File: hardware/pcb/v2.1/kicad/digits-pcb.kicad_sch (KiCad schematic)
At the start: 49 parts, among them J1 Conn_02x20_Odd_Even, J3 VIN_BARREL_PIGTAIL, J4 Conn_01x07, J6 Conn_01x02, J7 Screw_Terminal_01x02, J8 Conn_01x04, SW1 Hook_DPDT, SW2 SW_Push, U1 LM2596S-5, U3 RP2040, U4 W25Q16JVSSIQ, U5 AMS1117-3.3, Y1 ABM8-272-T3

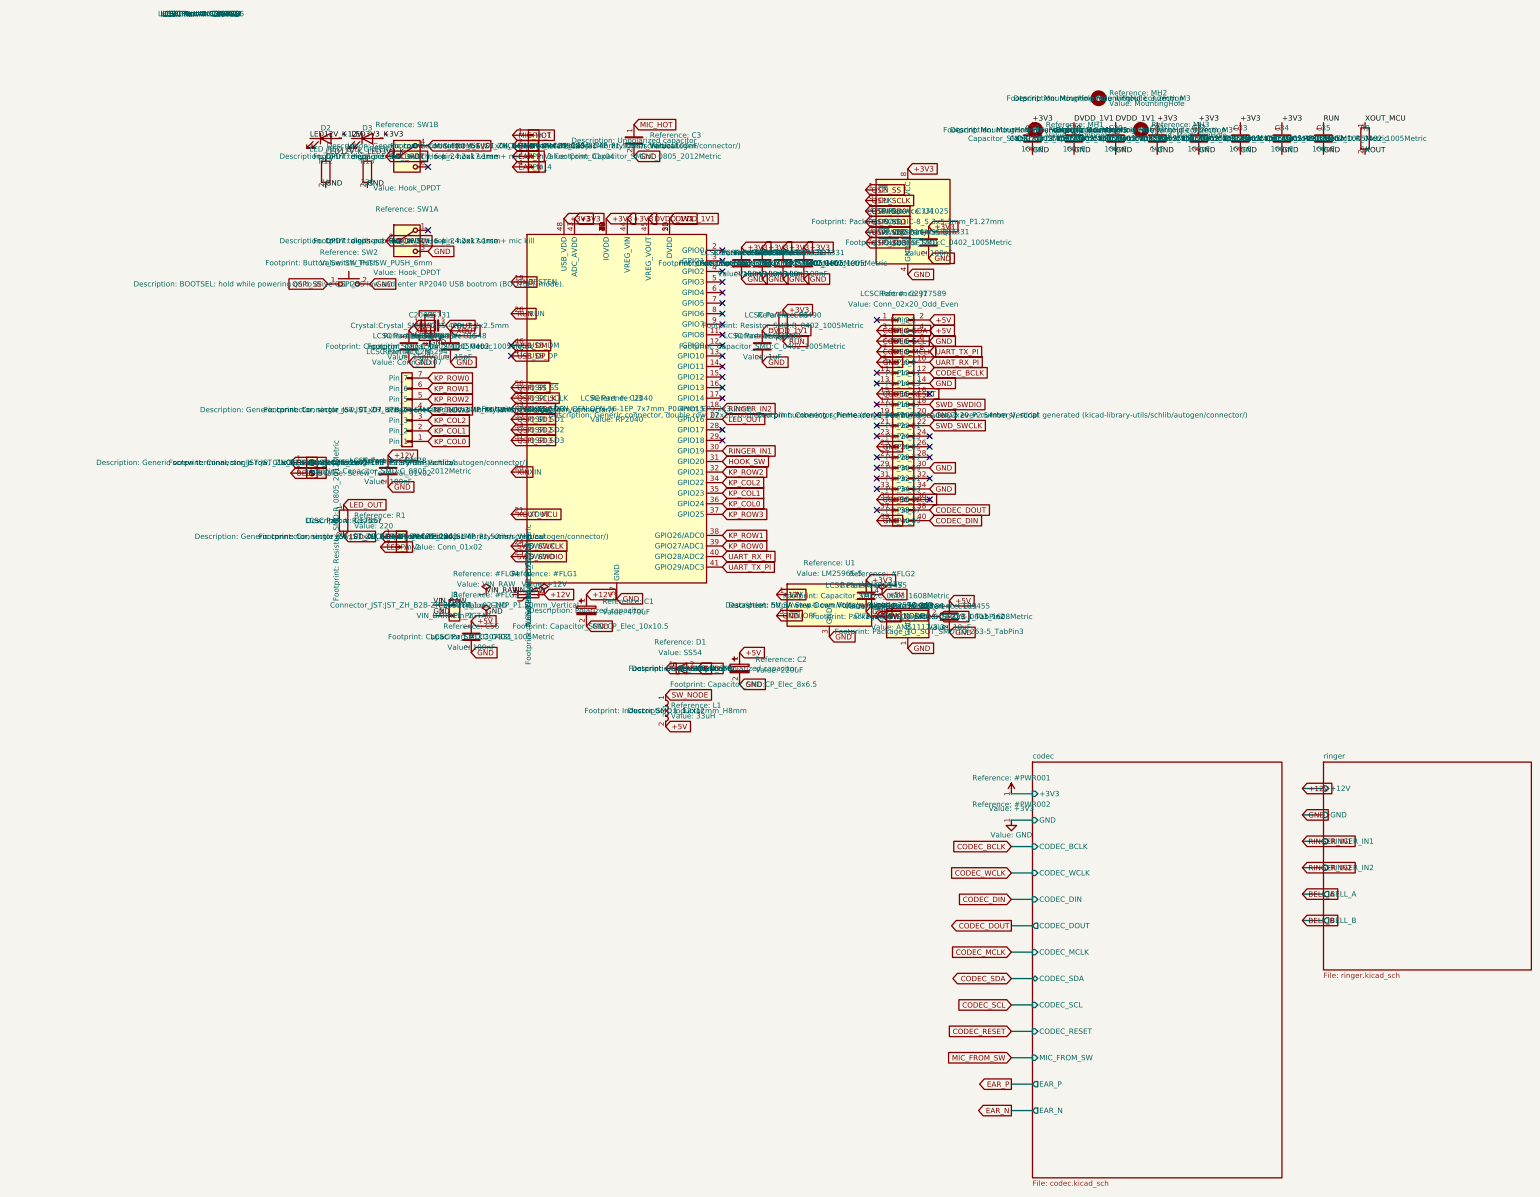
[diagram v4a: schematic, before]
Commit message: feat(hardware): switch to 5V input, drop buck stage, retarget boost to 37V
Bench testing confirmed the on-board boost approach matches the external
transformer for bell loudness: 79 dBA (transformer) vs 78 dBA (boost at 33V),
measured same distance/room/meter. The transformer is no longer justified.

Power input changed from 12V to 5V:
- Removed the entire LM2596 buck stage (U1, L1, D1, C2, C56). With 5V input
  there is nothing to buck down for the Pi; 5V feeds the Pi, the AMS1117 LDO,
  and the XL6019 boost directly.
- Merged the old +12V rail into +5V throughout both sheets.
- J3 connector kept as-is for now (barrel-jack pigtail); it will need a
  higher-current part since 5V at the same power draws ~2x the current.
- R12 (12V power LED resistor) changed 1k -> 300R to rebias for the 5V rail.

Boost output retargeted 42V -> 37V (R20 64.9k -> 57.6k, R21 unchanged at 2k):
- 37V gives 8V margin below the DRV8871's 45V VM limit (was only 3V at 42V).
- Bell already measured 78 dBA at 33V; 37V is marginally louder with far
  better headroom against inductive-kickback spikes.
- Lower boost ratio is also easier on the XL6019 from a 5V input.

PCB: boost cluster (U10/L10/D10/C100/C101/R20/R21) repositioned from the
off-board scratch area into the region between U2 and the codec. All
footprints on F.Cu. Layout and routing still in progress.

ERC clean (0 errors). Netlist: 77 components, +12V net fully eliminated,
codec subsheet intact (22 components).
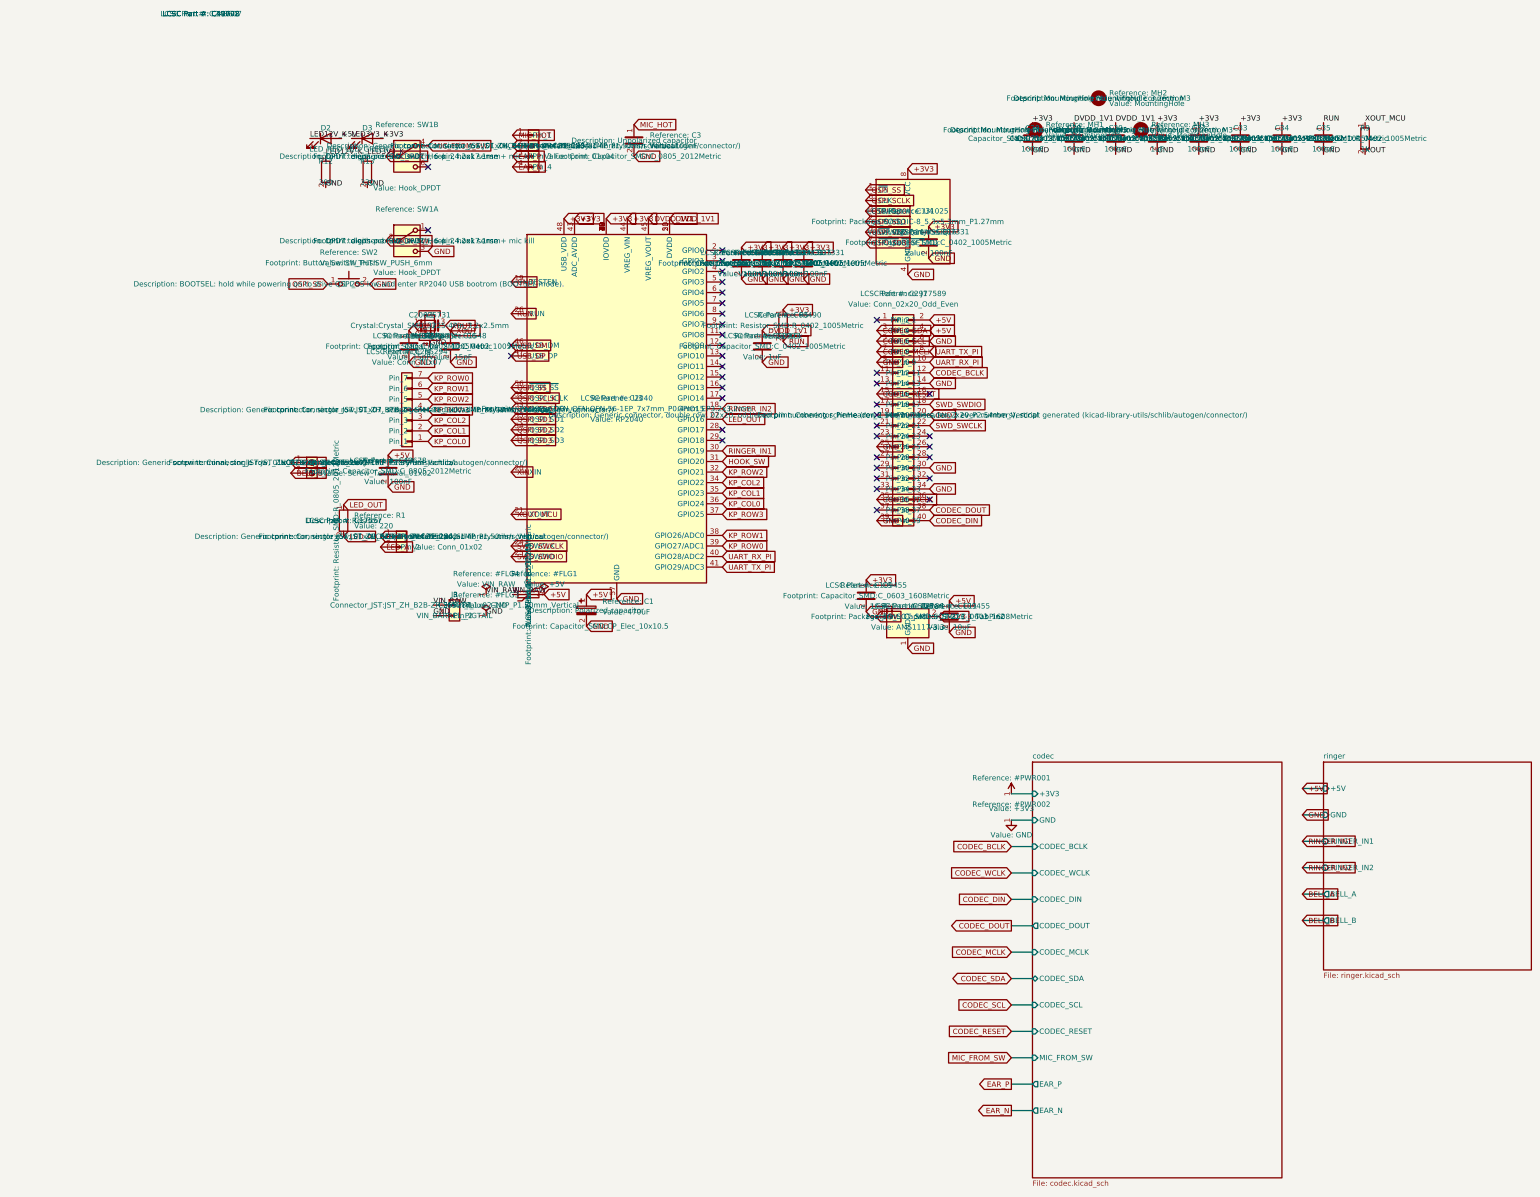
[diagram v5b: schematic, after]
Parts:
- removed C2: 220uF, Capacitor_SMD:CP_Elec_8x6.5, symbol Device:C_Polarized
- removed C56: 100nF, Capacitor_SMD:C_0402_1005Metric, symbol Device:C
- removed D1: SS54, Diode_SMD:D_SMA, symbol Device:D_Schottky
- removed L1: 33uH, Inductor_SMD:L_12x12mm_H8mm, symbol Device:L
- removed U1: LM2596S-5, Package_TO_SOT_SMD:TO-263-5_TabPin3, symbol Regulator_Switching:LM2596S-5
- R12: value 1k -> 300
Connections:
- net +12V is gone; now on net +5V: C1.1, C4.1, D2.2 (A), F1.2
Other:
- sheet ringer ports: added +5V; removed +12V

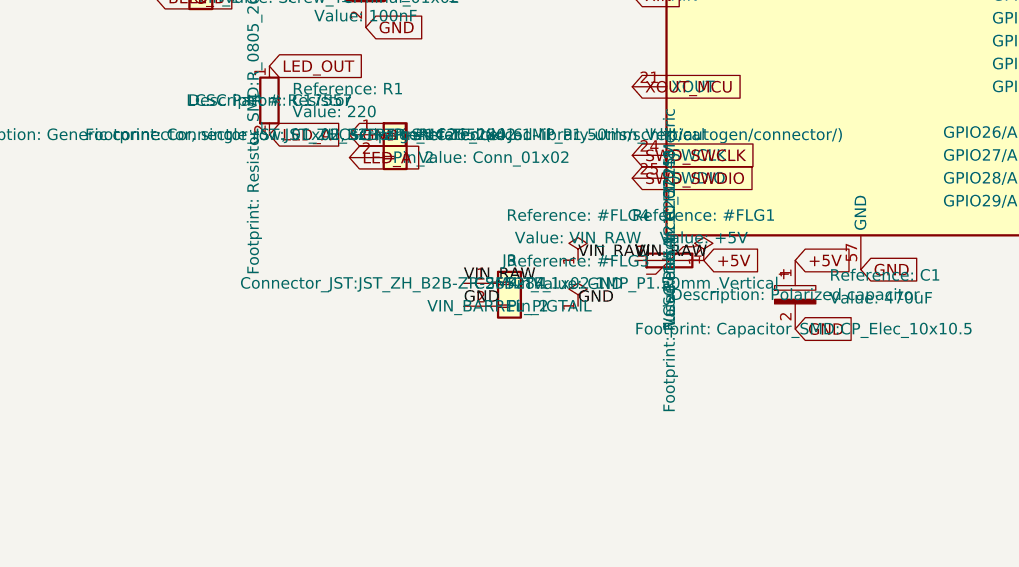
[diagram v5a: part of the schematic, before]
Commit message: fix(hardware): assign verified LCSC parts to boost components, fix J3 connector part
All boost-circuit components had empty LCSC Part # fields (JLCPCB would skip
them). Assigned in-stock, spec-verified parts:

- U10 XL6019E1 boost IC: C73018 (Basic)
- L10 47uH inductor: C9906 (Basic, 4.6A sat)
- D10 SS56 Schottky: C65009 (Basic)
- C100 100uF output bulk: C28241 (verified 63V, clears the 37V rail requirement)
- C101 1uF output HF: C105952 (100V X7R, no DC-bias derating concern at 37V)
- R20 feedback top: C26983 (57.6k 0402 1%, sets ~37V)
- R21 feedback bottom: C4109 (2k 0402 1%)

J3 LCSC corrected from C265284 (the old JST ZH part) to C158012 (genuine JST
B2B-XH-A, matches the XH footprint change). J6 and J7 deliberately left on
C265284 since they remain JST ZH.

SW2 (BOOTSEL tact) left without an LCSC part: 6mm THT tacts are all
low-stock/Extended on JLCPCB and trigger THT assembly fees for a button
pressed maybe twice in the board's life. Hand-mount.

ERC clean. Netlist confirms all assignments; J6/J7 unaffected.
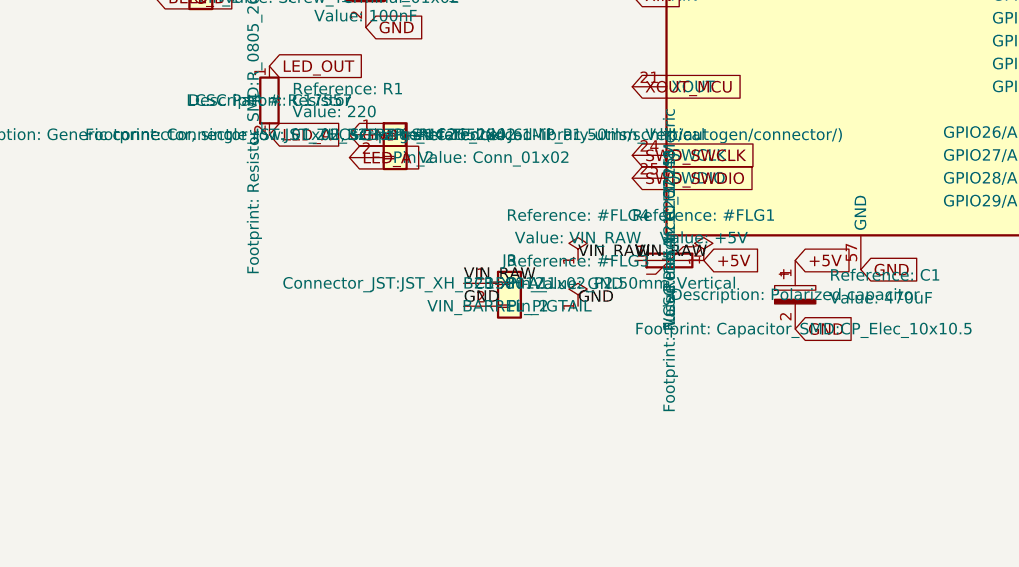
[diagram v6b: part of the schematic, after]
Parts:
- J3: footprint Connector_JST:JST_ZH_B2B-ZR-SM4-TF_1x02-1MP_P1.50mm_Vertical -> Connector_JST:JST_XH_B2B-XH-A_1x02_P2.50mm_Vertical; LCSC Part # C265284 -> C158012
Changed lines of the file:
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@@
 			)
 		)
-		(property "Footprint" "Connector_JST:JST_ZH_B2B-ZR-SM4-TF_1x02-1MP_P1.50mm_Vertical"
+		(property "Footprint" "Connector_JST:JST_XH_B2B-XH-A_1x02_P2.50mm_Vertical"
 			(at 60.96 142.24 0)
 			(show_name no)
@@
 			)
 		)
-		(property "LCSC Part #" "C265284"
+		(property "LCSC Part #" "C158012"
 			(at 60.96 142.24 0)
 			(show_name no)

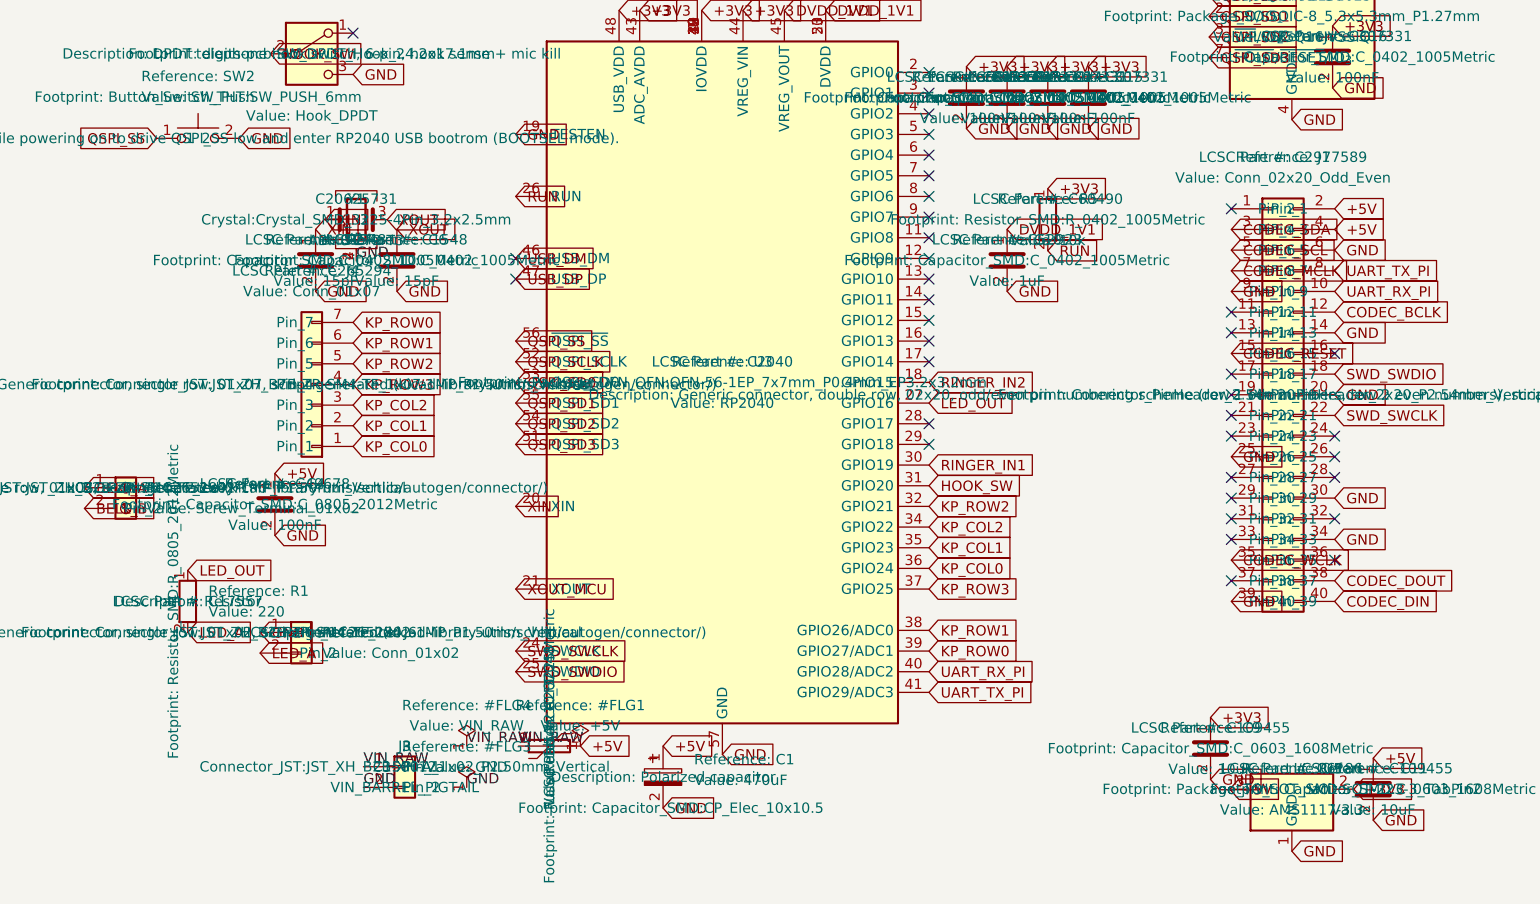
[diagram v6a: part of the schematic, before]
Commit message: fix(hardware): sync connector refs across sch/pcb, clean pre-fab defects
Rename connectors to semantic references in both schematic and PCB so the
two stay consistent: PWR, LED, KEYPAD, BELL, "Pi Zero W 2". Update the
baked unconnected-net placeholder names on the Pi header to match. Remove
a dangling via stub on the XIN crystal net, and add two GND vias to the
DRV8871 (U2) exposed pad for a lower-inductance ground tie.

DRC clean: 0 errors, 0 unconnected, 0 schematic-parity issues.
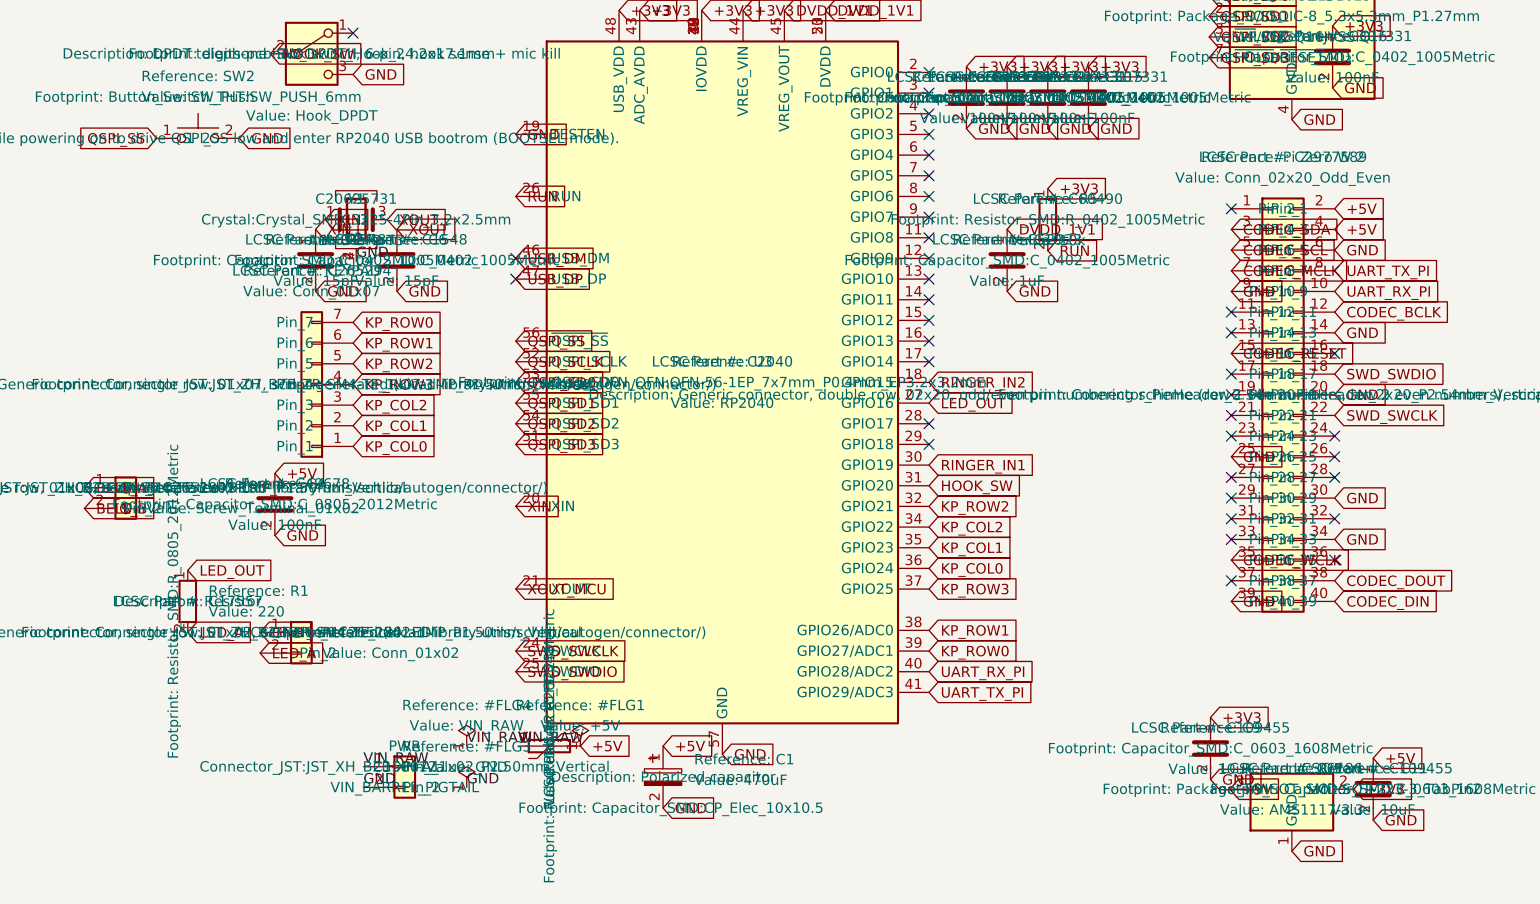
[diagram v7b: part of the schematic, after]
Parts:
- Pi Zero W 2: renamed from J1
- renumbered J7 to BELL, J4 to KEYPAD, J6 to LED, J3 to PWR
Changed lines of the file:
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@@
 		(dnp no)
 		(fields_autoplaced yes)
-		(property "Reference" "J7"
+		(property "Reference" "BELL"
 			(at 29.21 107.9499 0)
 			(show_name yes)
@@
 			(project "digits-pcb"
 				(path "/74ec24e7-a8af-4132-928f-b03228b07139"
-					(reference "J7")
+					(reference "BELL")
 					(unit 1)
 				)
@@
 		(in_pos_files yes)
 		(dnp no)
-		(property "Reference" "J3"
+		(property "Reference" "PWR"
 			(at 60.96 139.7 0)
 			(show_name no)
@@
 			(project "digits-pcb"
 				(path "/74ec24e7-a8af-4132-928f-b03228b07139"
-					(reference "J3")
+					(reference "PWR")
 					(unit 1)
 				)
@@
 		(dnp no)
 		(fields_autoplaced yes)
-		(property "Reference" "J6"
+		(property "Reference" "LED"
 			(at 50.8 125.7299 0)
 			(show_name yes)
@@
 			(project "digits-pcb"
 				(path "/74ec24e7-a8af-4132-928f-b03228b07139"
-					(reference "J6")
+					(reference "LED")
 					(unit 1)
 				)
@@
 		(dnp no)
 		(fields_autoplaced yes)
-		(property "Reference" "J1"
+		(property "Reference" "Pi Zero W 2"
 			(at 168.91 67.31 0)
 			(show_name yes)
@@
 			(project "digits-pcb"
 				(path "/74ec24e7-a8af-4132-928f-b03228b07139"
-					(reference "J1")
+					(reference "Pi Zero W 2")
 					(unit 1)
 				)
@@
 		(dnp no)
 		(fields_autoplaced yes)
-		(property "Reference" "J4"
+		(property "Reference" "KEYPAD"
 			(at 49.53 81.28 0)
 			(show_name yes)
@@
 			(project "digits-pcb"
 				(path "/74ec24e7-a8af-4132-928f-b03228b07139"
-					(reference "J4")
-					(unit 1)
-				)
+					(reference "KEYPAD")
+					(unit 1)
+				)
